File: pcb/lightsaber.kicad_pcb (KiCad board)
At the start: 2 copper layers, 107.6 x 27.9 mm, 1 part

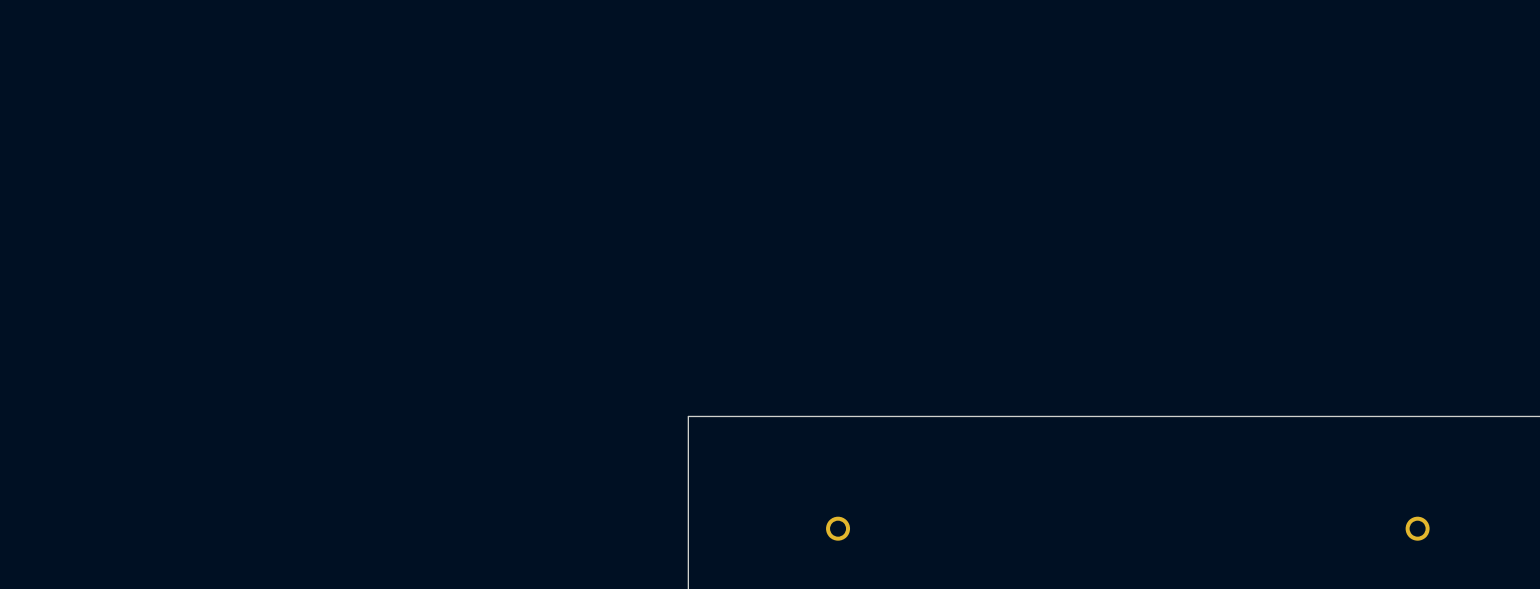
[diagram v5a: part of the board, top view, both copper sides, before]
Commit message: Laptop footprints
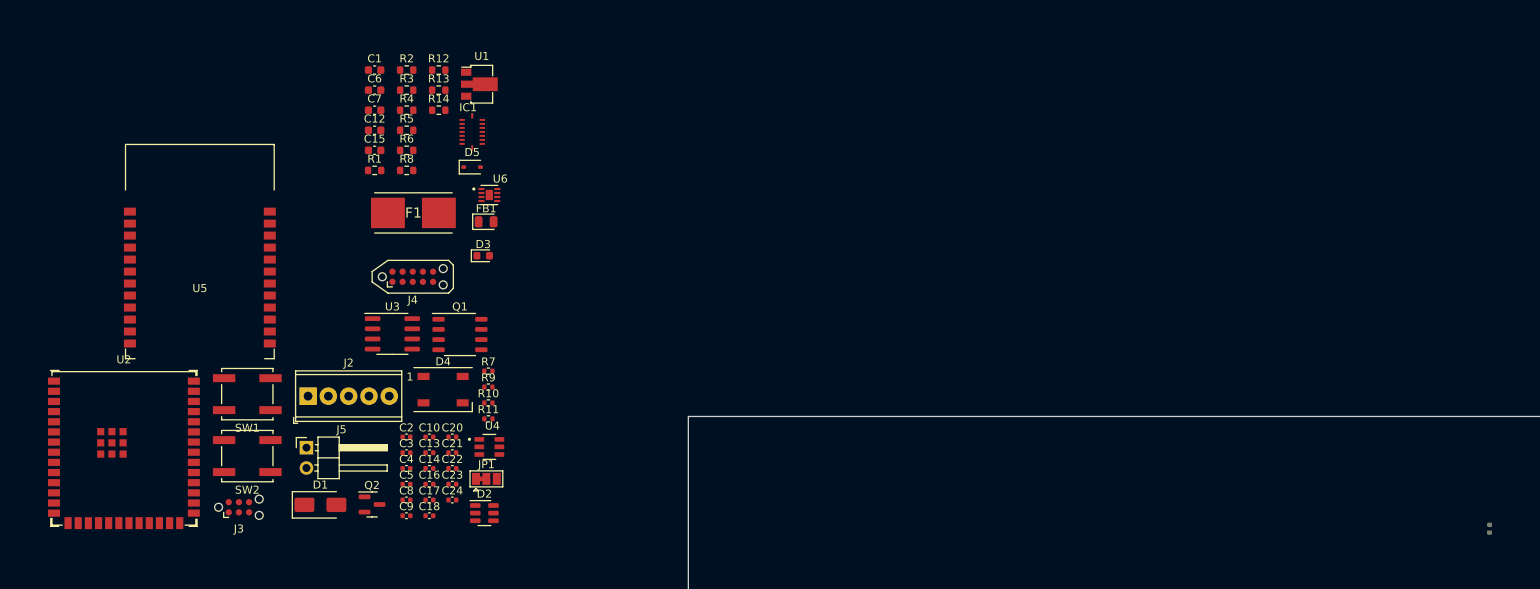
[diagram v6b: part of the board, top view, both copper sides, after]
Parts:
- added C1: 10uF, Capacitor_SMD:C_0603_1608Metric, F.Cu at (84.0, 37.6)
- added C10: 100nF, Capacitor_SMD:C_0402_1005Metric, F.Cu at (90.9, 83.5)
- added C12: 10uF, Capacitor_SMD:C_0603_1608Metric, F.Cu at (84.0, 45.2)
- added C13: 1uF, Capacitor_SMD:C_0402_1005Metric, F.Cu at (90.9, 85.5)
- added C14: 1uF, Capacitor_SMD:C_0402_1005Metric, F.Cu at (90.9, 87.5)
- added C15: 10uF, Capacitor_SMD:C_0603_1608Metric, F.Cu at (84.0, 47.7)
- added C16: 1nF, Capacitor_SMD:C_0402_1005Metric, F.Cu at (90.9, 89.4)
- added C17: 4.7nF, Capacitor_SMD:C_0402_1005Metric, F.Cu at (90.9, 91.4)
- added C18: 1uF, Capacitor_SMD:C_0402_1005Metric, F.Cu at (90.9, 93.4)
- added C2: 1uF, Capacitor_SMD:C_0402_1005Metric, F.Cu at (88.0, 83.5)
- added C20: 100nF, Capacitor_SMD:C_0402_1005Metric, F.Cu at (93.8, 83.5)
- added C21: 1uF, Capacitor_SMD:C_0402_1005Metric, F.Cu at (93.8, 85.5)
- added C22: 1uF, Capacitor_SMD:C_0402_1005Metric, F.Cu at (93.8, 87.5)
- added C23: 1uF, Capacitor_SMD:C_0402_1005Metric, F.Cu at (93.8, 89.4)
- added C24: 1uF, Capacitor_SMD:C_0402_1005Metric, F.Cu at (93.8, 91.4)
- added C3: 100nF, Capacitor_SMD:C_0402_1005Metric, F.Cu at (88.0, 85.5)
- added C4: 1uF, Capacitor_SMD:C_0402_1005Metric, F.Cu at (88.0, 87.5)
- added C5: 1uF, Capacitor_SMD:C_0402_1005Metric, F.Cu at (88.0, 89.4)
- added C6: 10uF, Capacitor_SMD:C_0603_1608Metric, F.Cu at (84.0, 40.1)
- added C7: 10uF, Capacitor_SMD:C_0603_1608Metric, F.Cu at (84.0, 42.6)
- added C8: 1uF, Capacitor_SMD:C_0402_1005Metric, F.Cu at (88.0, 91.4)
- added C9: 100nF, Capacitor_SMD:C_0402_1005Metric, F.Cu at (88.0, 93.4)
- added D1: Schottky, Diode_SMD:D_SMA, F.Cu at (77.2, 92.0)
- added D2: SP0505BAHT, Package_TO_SOT_SMD:SOT-23-6, F.Cu at (97.8, 93.0)
- added D3: LED, LED_SMD:LED_0603_1608Metric, F.Cu at (97.6, 60.9)
- added D4: WS2812B, LED_SMD:LED_WS2812B_PLCC4_5.0x5.0mm_P3.2mm, F.Cu at (92.6, 77.6)
- added D5: 1N4148, Diode_SMD:D_SOD-323, F.Cu at (96.2, 49.8)
- added F1: 8A Fuse, Littelfuse:0154008DR, F.Cu at (88.9, 55.5)
- added FB1: FerriteBead, Diode_SMD:D_0805_2012Metric, F.Cu at (98.0, 56.6)
- added IC1: BMI055, BMI:QFN50P300X450X100-16N, F.Cu at (96.2, 45.4)
- added J2: Screw_Terminal_01x05, TerminalBlock_Phoenix:TerminalBlock_Phoenix_MPT-0,5-5-2.54_1x05_P2.54mm_Horizontal, F.Cu at (75.7, 78.4)
- added J3: ESP32 Prog, Connector:Tag-Connect_TC2030-IDC-NL_2x03_P1.27mm_Vertical, F.Cu at (67.1, 92.3)
- added J4: ESP32 JTAG, Connector:Tag-Connect_TC2050-IDC-NL_2x05_P1.27mm_Vertical_with_bottom_clip, F.Cu at (88.8, 63.5)
- added J5: Conn_01x02, Connector_PinHeader_2.54mm:PinHeader_1x02_P2.54mm_Horizontal, F.Cu at (75.5, 84.9)
- added JP1: 10k Bridge, Jumper:SolderJumper-3_P1.3mm_Bridged12_Pad1.0x1.5mm, F.Cu at (98.0, 88.8)
- added Q1: PMOS, Package_SO:SSOP-8_3.9x5.05mm_P1.27mm, F.Cu at (94.7, 70.7)
- added Q2: NPN, Package_TO_SOT_SMD:SOT-23, F.Cu at (83.7, 92.0)
- added R1: 5.1k, Resistor_SMD:R_0603_1608Metric, F.Cu at (84.0, 50.2)
- added R10: 4.7k, Resistor_SMD:R_0402_1005Metric, F.Cu at (98.3, 79.3)
- added R11: 10R, Resistor_SMD:R_0402_1005Metric, F.Cu at (98.3, 81.3)
- added R12: 10k, Resistor_SMD:R_0603_1608Metric, F.Cu at (92.1, 37.6)
- added R13: 10k, Resistor_SMD:R_0603_1608Metric, F.Cu at (92.1, 40.1)
- added R14: 10k, Resistor_SMD:R_0603_1608Metric, F.Cu at (92.1, 42.6)
- added R2: 5.1k, Resistor_SMD:R_0603_1608Metric, F.Cu at (88.0, 37.6)
- added R3: 100k, Resistor_SMD:R_0603_1608Metric, F.Cu at (88.0, 40.1)
- added R4: 1k, Resistor_SMD:R_0603_1608Metric, F.Cu at (88.0, 42.6)
- added R5: 10k, Resistor_SMD:R_0603_1608Metric, F.Cu at (88.0, 45.2)
- added R6: 1k, Resistor_SMD:R_0603_1608Metric, F.Cu at (88.0, 47.7)
- added R7: 10k, Resistor_SMD:R_0402_1005Metric, F.Cu at (98.3, 75.3)
- added R8: 1k, Resistor_SMD:R_0603_1608Metric, F.Cu at (88.0, 50.2)
- added R9: 4.7k, Resistor_SMD:R_0402_1005Metric, F.Cu at (98.3, 77.3)
- added SW1: SW_Push, Button_Switch_SMD:SW_Push_1P1T_NO_CK_KSC6xxJ, F.Cu at (68.1, 78.2)
- added SW2: SW_Push, Button_Switch_SMD:SW_Push_1P1T_NO_CK_KSC6xxJ, F.Cu at (68.1, 85.9)
- added U1: ME6211A33PG-N, Package_TO_SOT_SMD:SOT-89-3, F.Cu at (97.4, 39.4)
- added U2: ESP32-S3-WROOM-1, Espressif:ESP32-S3-WROOM-1U, F.Cu at (52.7, 84.8)
- added U3: ACS725xLCTR-10AU, Package_SO:SOIC-8_3.9x4.9mm_P1.27mm, F.Cu at (86.3, 70.6)
- added U4: BQ21040DBVR, BQ21040:SOT95P280X145-6N, F.Cu at (98.4, 84.8)
- added U5: 5994, CityTheatrical:Module 5994, F.Cu at (62.2, 65.4)
- added U6: MAX17048G+T10, MAX17048:SON50P200X200X80-9N, F.Cu at (98.4, 53.3)
- C11: value 18650 Holder -> 100nF; footprint Sams Library:18650-Holder -> Capacitor_SMD:C_0402_1005Metric
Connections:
- C11 pad 1: +BATT -> +3.3V

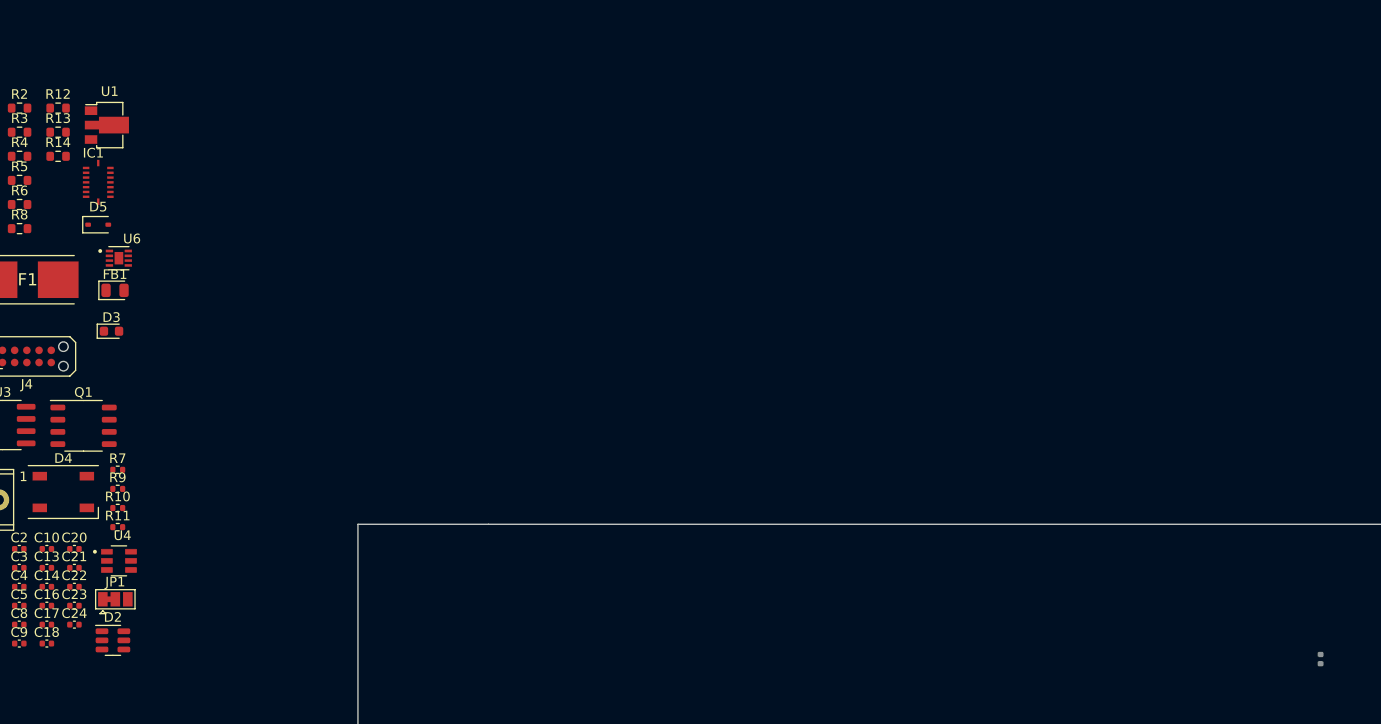
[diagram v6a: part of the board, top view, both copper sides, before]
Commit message: All symbols imported
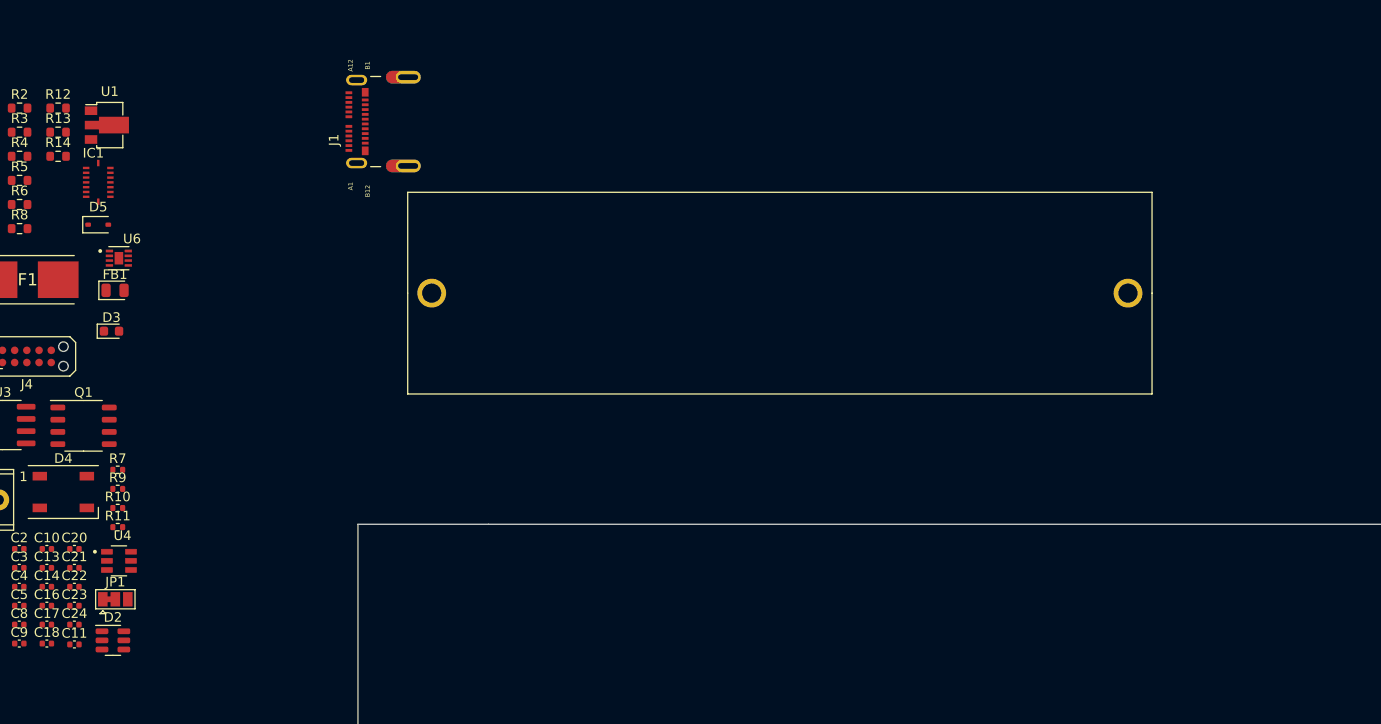
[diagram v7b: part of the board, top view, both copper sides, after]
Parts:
- added C19: 18650 Holder, Sams Library:18650-Holder, F.Cu at (122.0, 56.9)
- added J1: 2012670005, Molex:MOLEX_2012670005, F.Cu at (123.1, 39.0)
- C11: moved to F.Cu
- moved C11 129.8 mm to (93.8, 93.5), turned to 0 degrees
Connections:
- IC1 pad 2: (no net) -> unconnected-(IC1-NC-Pad2)

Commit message: Completed design
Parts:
- removed C18: 1uF, Capacitor_SMD:C_0402_1005Metric
- removed U5: 5994, CityTheatrical:Module 5994
- added G***: LOGO, LOGO, B.Cu at (202.7, 82.3)
- added J6: Conn_01x06, Connector_PinHeader_2.54mm:PinHeader_1x06_P2.54mm_Vertical, B.Cu at (177.4, 98.2)
- C19, D4, J2: moved to B.Cu
- J5: footprint Connector_PinHeader_2.54mm:PinHeader_1x02_P2.54mm_Horizontal -> TerminalBlock_Phoenix:TerminalBlock_Phoenix_MPT-0,5-2-2.54_1x02_P2.54mm_Horizontal; moved to B.Cu
- moved J5 141.7 mm to (217.0, 77.5), turned to -90 degrees
- moved J2 141.4 mm to (217.0, 84.0), turned to -90 degrees
- moved Q2 127.0 mm to (209.6, 75.2), turned to -90 degrees
- moved SW1 126.8 mm to (194.0, 93.2), turned to 180 degrees
- moved SW2 126.1 mm to (194.0, 78.5)
- moved R8 121.5 mm to (207.0, 74.8), turned to 90 degrees
- moved U3 120.4 mm to (204.5, 93.5), turned to 180 degrees
- moved F1 119.2 mm to (204.5, 84.3), turned to 90 degrees
- moved D5 119.0 mm to (212.5, 75.1), turned to 90 degrees
- moved U2 118.7 mm to (171.4, 86.3), turned to 180 degrees
- moved R14 117.8 mm to (205.4, 74.8), turned to 90 degrees
- moved C21 116.8 mm to (210.6, 88.8)
- moved R11 114.3 mm to (212.5, 77.3), turned to 180 degrees
- moved R7 113.2 mm to (210.6, 89.8), turned to 180 degrees
- moved C9 112.8 mm to (200.8, 96.9), turned to 180 degrees
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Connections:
- net Net-(C19-VBAT) renamed /BAT_FUSE
- net Net-(JP1-C) renamed /BQ_TS_JUMP
- net Net-(Q2-B) renamed /MOTOR_TRANSISTOR
- net Net-(U3-FILTER) renamed /ACS_FILTER
- net Net-(U4-ISET) renamed /BQ_ISET
- net Net-(U4-TS) renamed /BQ_TS
- D3 pad 1: Net-(D3-K) -> /CHG_LED
- D3 pad 2: /CHG_LED -> /CHG_LED_RES
- D5 pad 1: Net-(D5-K) -> /MOTOR_POS
- D5 pad 2: Net-(D5-A) -> /MOTOR_NEG
- J2 pad 1: LED_PWR -> GND
- J2 pad 2: ESP_LED_DATA -> ESP_USER_BUTTON
- J2 pad 4: ESP_USER_BUTTON -> ESP_LED_DATA
- J2 pad 5: GND -> LED_PWR
- J5 pad 1: Net-(D5-K) -> /MOTOR_NEG
- J5 pad 2: Net-(D5-A) -> /MOTOR_POS
- Q2 pad 1: Net-(D5-A) -> /MOTOR_NEG
- R11 pad 1: Net-(D5-K) -> /MOTOR_POS
- R11 pad 2: +3.3V -> +BATT
- R4 pad 2: /CHG_LED -> /CHG_LED_RES
- U2 pad 4: ESP32_BMI_GYRO_1 -> ESP32_BMI_ACCEL_2
- U2 pad 5: ESP32_BMI_GYRO_2 -> ESP32_BMI_GYRO_1
- U2 pad 7: ESP32_BMI_ACCEL_2 -> ESP32_BMI_GYRO_2
- U4 pad 3: Net-(D3-K) -> /CHG_LED
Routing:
- net +BATT: track 0.00 -> 105.0 mm
- net GND: track 0.00 -> 95.6 mm, vias 0 -> 41
- net ESP_IO0: track 0.00 -> 95.1 mm, vias 0 -> 3
- net ESP_EN: track 0.00 -> 80.5 mm
- net ESP32_I2C_SCL: track 0.00 -> 62.7 mm, vias 0 -> 4
- net D-: track 0.00 -> 62.3 mm, vias 0 -> 5
- net D+: track 0.00 -> 61.0 mm, vias 0 -> 5
- net ESP32_I2C_SDA: track 0.00 -> 60.5 mm, vias 0 -> 2
- net ESP_USER_BUTTON: track 0.00 -> 58.7 mm, vias 0 -> 4
- net ESP_LED_DEBUG: track 0.00 -> 57.5 mm, vias 0 -> 1
- net VDD: track 0.00 -> 52.2 mm
- net ESP_MOTOR: track 0.00 -> 43.2 mm, vias 0 -> 2
- net ESP_CURRENT_SENSE: track 0.00 -> 43.1 mm, vias 0 -> 2
- net ESP_TDI: track 0.00 -> 41.4 mm, vias 0 -> 2
- net ESP_UART_TX: track 0.00 -> 41.3 mm
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- added copper zone on In2.Cu, net +3.3V
- added copper zone on F.Cu, net +BATT
- added copper zone on F.Cu, net GND
- added copper zone on In1.Cu, net GND
- added copper zone on F.Cu, net LED_PWR
- added copper zone on F.Cu, net VCC
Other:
- board size 107.6 x 27.9 mm -> 100 x 28 mm
- copper layers 2 -> 4
- board text added: "."
- board text added: "BTTF Lightsaber: v2.5 Firmware: v Sam Lane"
